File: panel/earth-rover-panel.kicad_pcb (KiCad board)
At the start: 2 copper layers, 212.1 x 101.6 mm, 107 parts, among them J1 Conn_01x04_Male, J1 Conn_02x04_Male_UnitPerRow, J10 Connector:Screw_Terminal_01x02, J2 Conn_01x04_Male, J3 Conn_01x04_Male, J3 Conn_02x03_Male, J4 Conn_01x04_Male, J4 Conn_02x03_Male, J5 5.4mm/2.5mm, J5 Conn_02x03_Male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

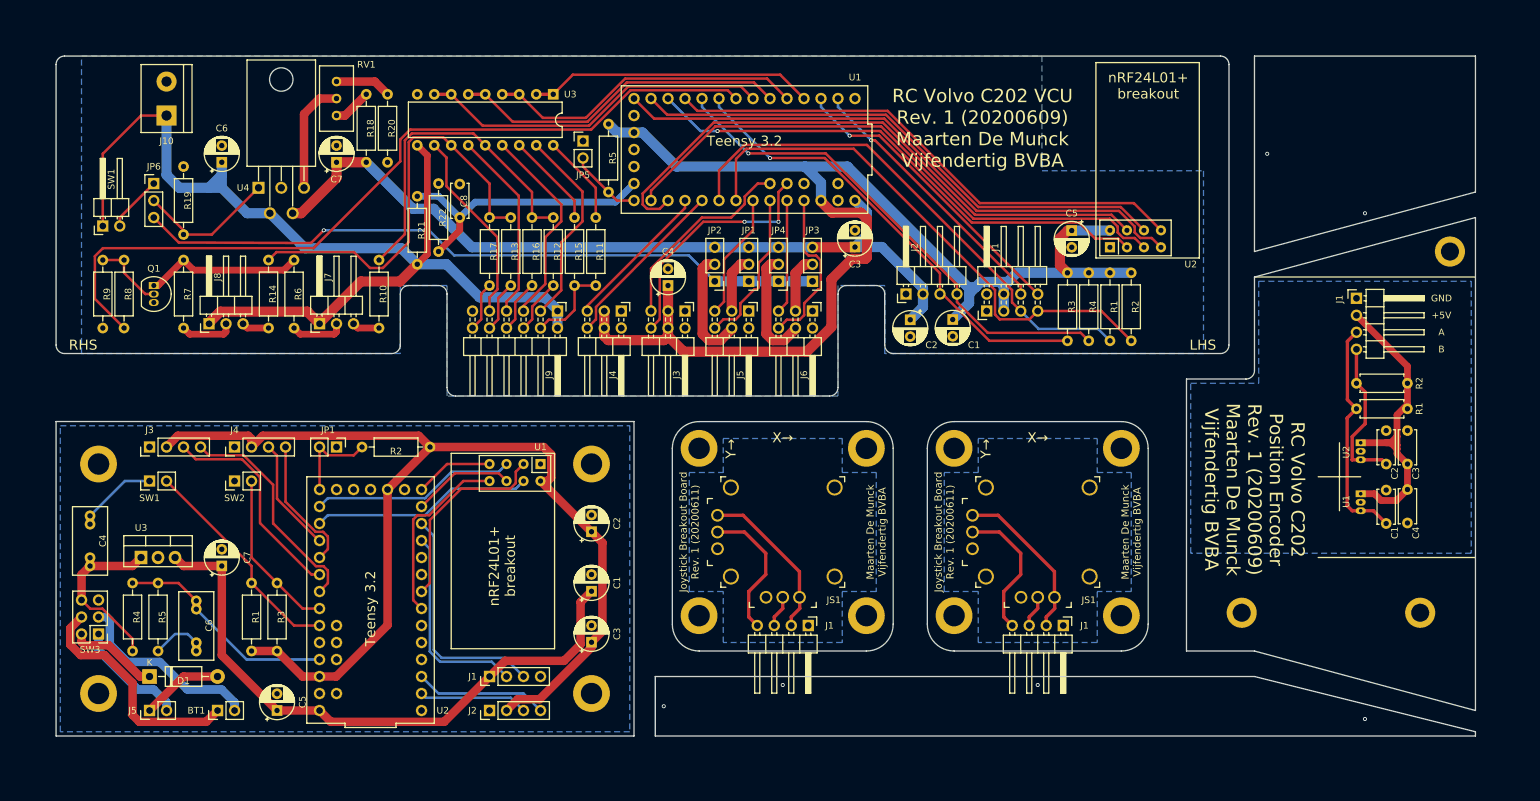
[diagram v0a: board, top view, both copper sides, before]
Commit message: Update panel according to Eurocircuits' specifications
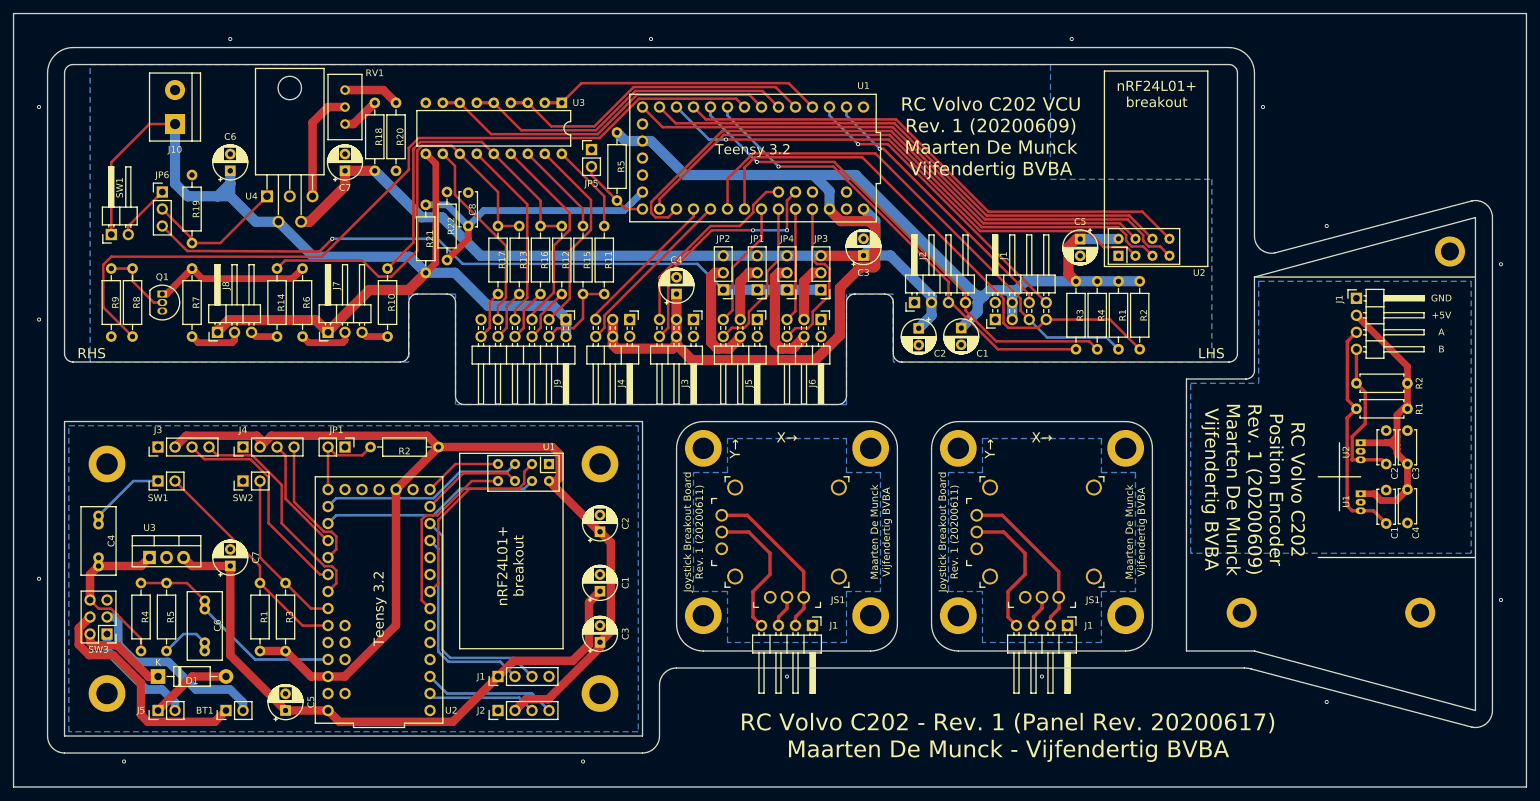
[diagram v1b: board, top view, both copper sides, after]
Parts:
- removed the REF** at (189.2, 137.2)
- removed the REF** at (189.2, 171.4)
- added REF**: MountingHole_3.2mm_M3_ISO14580_Pad, MountingHole:MountingHole_3.2mm_M3_ISO14580_Pad, F.Cu at (190.5, 137.2)
- added REF**: MountingHole_3.2mm_M3_ISO14580_Pad, MountingHole:MountingHole_3.2mm_M3_ISO14580_Pad, F.Cu at (190.5, 171.4)
- moved R1 1.80 mm to (268.0, 109.9)
- moved R4 1.80 mm to (264.8, 109.9)
- moved U2 1.80 mm to (268.0, 106.0)
- moved C4 1.80 mm to (201.9, 111.8)
- moved R12 1.80 mm to (184.8, 111.8)
- moved R13 1.80 mm to (178.4, 111.8)
- moved R15 1.80 mm to (188.0, 111.8)
- moved R16 1.80 mm to (181.6, 111.8)
- moved C2 1.80 mm to (238.1, 116.9)
- moved C3 1.80 mm to (229.9, 106.0)
- moved C7 1.80 mm to (152.4, 93.3)
- moved C8 1.80 mm to (170.8, 101.6)
- moved J1 1.80 mm to (249.6, 115.6)
- moved J2 1.80 mm to (237.5, 113.0)
- moved J3 1.80 mm to (204.5, 115.6)
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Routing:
- net (no net): vias 6 -> 15
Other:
- board size 212.1 x 101.6 mm -> 226.1 x 115.6 mm
- board text added: "RC Volvo C202 - Rev. 1 (Panel Rev. 20200617) Maarten De Munck - Vijfendertig BVBA"

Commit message: Use larger holes for nRF24L01+ breakout board
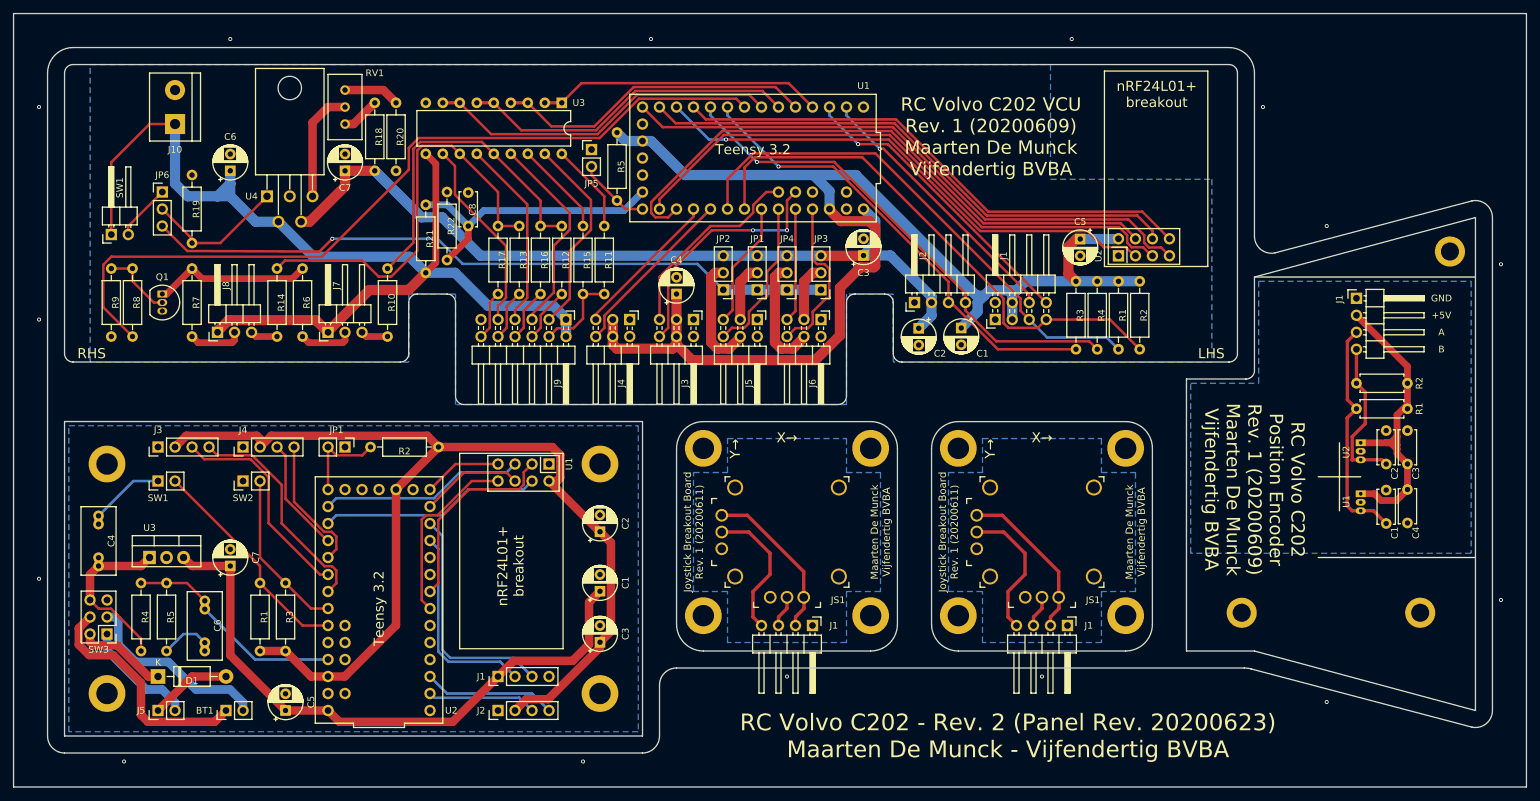
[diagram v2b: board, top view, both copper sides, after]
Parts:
- U1, U2: footprint RF_Module:nRF24L01_Breakout -> earth-rover-footprints:nRF24L01_Breakout_LargerHoles
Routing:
- net /NRF24L01_MOSI: track 97.0 -> 97.8 mm
- net +BATT: vias 0 -> 1
- net (no net): vias 15 -> 14
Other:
- net class Default: clearance 0.25 -> 0.2; trace_width 0.25 -> 0.381
- net class Wide removed
- rule pad_to_mask_clearance: 0.051 -> 0.05
- rule trace_clearance: 0.25 -> 0.2
- board text added: "RC Volvo C202 - Rev. 2 (Panel Rev. 20200623) Maarten De Munck - Vijfendertig BVBA"
- board text removed: "RC Volvo C202 - Rev. 1 (Panel Rev. 20200617) Maarten De Munck - Vijfendertig BVBA"
